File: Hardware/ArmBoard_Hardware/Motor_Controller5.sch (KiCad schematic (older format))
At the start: 13 parts

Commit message: added missing lables to connectors
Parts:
- MC5: symbol MRDT_ICs:VNH5019A_E -> ArmBoard_Hardware-rescue:VNH5019A_E-MRDT_ICs
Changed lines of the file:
@@
 IN_A_5
 $Comp
-L MRDT_ICs:VNH5019A_E U?
+L ArmBoard_Hardware-rescue:VNH5019A_E-MRDT_ICs U?
 U 1 1 630AB847
 P 4925 4600

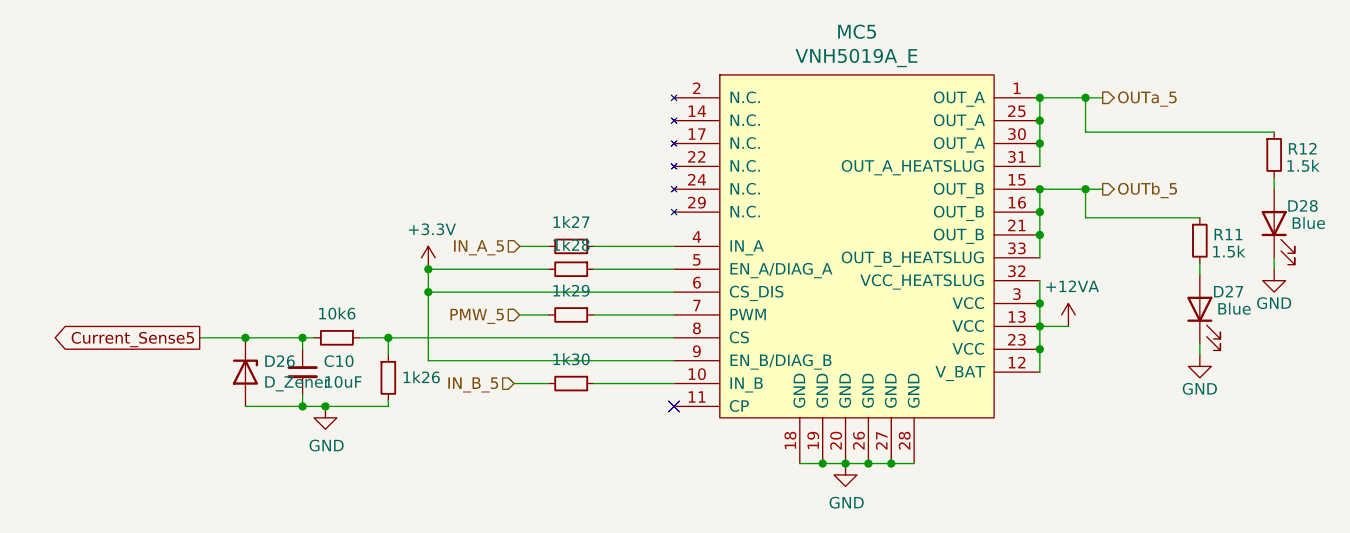
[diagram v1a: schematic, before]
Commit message: schematic changes, encoder changes, led changes
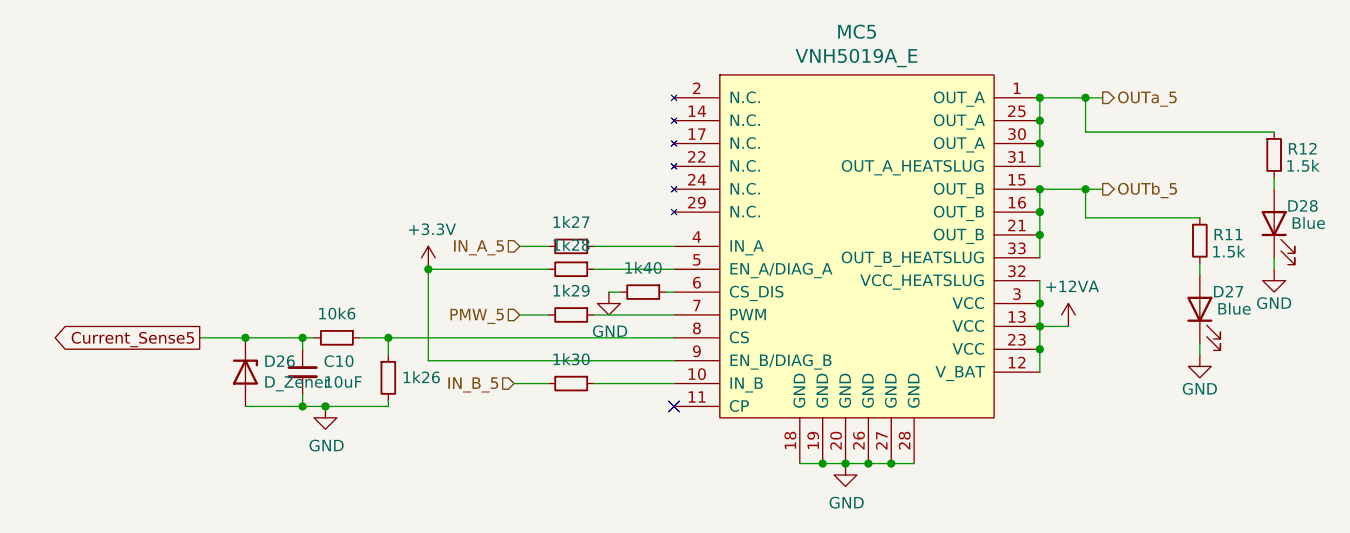
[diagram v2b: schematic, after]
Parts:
- added 1k40: R_Small, Resistor_SMD:R_0603_1608Metric_Pad0.98x0.95mm_HandSolder, symbol Device:R_Small
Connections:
- net +3V3: no longer MC5.6 (CS_DIS)
- net GND: now also 1k40.2
- new net: 1k40.1, MC5.6 (CS_DIS)
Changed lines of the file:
@@
 Wire Wire Line
 	4175 4150 4050 4150
-Wire Wire Line
-	4725 4050 3650 4050
-Wire Wire Line
-	3650 4050 3650 3950
 Connection ~ 3650 3950
 Wire Wire Line
 	4725 4350 3650 4350
-Wire Wire Line
-	3650 4350 3650 4050
-Connection ~ 3650 4050
 Wire Wire Line
 	4725 4250 3475 4250
@@
 Text HLabel 6600 3600 2    50   Output ~ 0
 OUTb_5
+Wire Wire Line
+	3650 3950 3650 4350
+$Comp
+L power:GND #PWR?
+U 1 1 629144E4
+P 4440 4050
+AR Path="/63845F20/629144E4" Ref="#PWR?"  Part="1"
+AR Path="/628CE14B/629144E4" Ref="#PWR?"  Part="1"
+AR Path="/6297969A/629144E4" Ref="#PWR?"  Part="1"
+AR Path="/629F46F6/629144E4" Ref="#PWR?"  Part="1"
+AR Path="/629F46FD/629144E4" Ref="#PWR?"  Part="1"
+AR Path="/62A5CC3B/629144E4" Ref="#PWR?"  Part="1"
+AR Path="/62A5CC46/629144E4" Ref="#PWR?"  Part="1"
+AR Path="/62AF9C52/629144E4" Ref="#PWR?"  Part="1"
+AR Path="/62D2CE1B/629144E4" Ref="#PWR?"  Part="1"
+AR Path="/62D3BCB9/629144E4" Ref="#PWR09"  Part="1"
+F 0 "#PWR09" H 4440 3800 50  0001 C CNN
+F 1 "GND" H 4445 3877 50  0000 C CNN
+F 2 "" H 4440 4050 50  0001 C CNN
+F 3 "" H 4440 4050 50  0001 C CNN
+	1    4440 4050
+	1    0    0    -1
+$EndComp
+$Comp
+L Device:R_Small 1k?
+U 1 1 629144EA
+P 4590 4050
+AR Path="/63845F20/629144EA" Ref="1k?"  Part="1"
+AR Path="/628CE14B/629144EA" Ref="1k?"  Part="1"
+AR Path="/6297969A/629144EA" Ref="1k?"  Part="1"
+AR Path="/629F46F6/629144EA" Ref="1k?"  Part="1"
+AR Path="/629F46FD/629144EA" Ref="1k?"  Part="1"
+AR Path="/62A5CC3B/629144EA" Ref="1k?"  Part="1"
+AR Path="/62A5CC46/629144EA" Ref="1k?"  Part="1"
+AR Path="/62AF9C52/629144EA" Ref="1k?"  Part="1"
+AR Path="/62C19165/629144EA" Ref="1k?"  Part="1"
+AR Path="/62CA8FD7/629144EA" Ref="1k?"  Part="1"
+AR Path="/62CBA1AC/629144EA" Ref="1k?"  Part="1"
+AR Path="/62CCE879/629144EA" Ref="1k?"  Part="1"
+AR Path="/62CE0B38/629144EA" Ref="1k?"  Part="1"
+AR Path="/62CF1227/629144EA" Ref="1k?"  Part="1"
+AR Path="/62D0C672/629144EA" Ref="1k?"  Part="1"
+AR Path="/62D1BEB1/629144EA" Ref="1k?"  Part="1"
+AR Path="/62D2CE1B/629144EA" Ref="1k?"  Part="1"
+AR Path="/62D3BCB9/629144EA" Ref="1k40"  Part="1"
+AR Path="/62D4BAA1/629144EA" Ref="1k?"  Part="1"
+F 0 "1k40" V 4486 4050 50  0000 C CNN
+F 1 "R_Small" V 4485 4050 50  0001 C CNN
+F 2 "Resistor_SMD:R_0603_1608Metric_Pad0.98x0.95mm_HandSolder" H 4590 4050 50  0001 C CNN
+F 3 "~" H 4590 4050 50  0001 C CNN
+	1    4590 4050
+	0    1    1    0
+$EndComp
+Wire Wire Line
+	4440 4050 4490 4050
+Wire Wire Line
+	4690 4050 4725 4050
 $EndSCHEMATC

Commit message: gerbs added and zipped
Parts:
- MC5: symbol ArmBoard_Hardware-rescue:VNH5019A_E-MRDT_ICs -> MRDT_ICs:VNH5019A_E
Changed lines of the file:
@@
 IN_A_5
 $Comp
-L ArmBoard_Hardware-rescue:VNH5019A_E-MRDT_ICs U?
+L MRDT_ICs:VNH5019A_E U?
 U 1 1 630AB847
 P 4925 4600
